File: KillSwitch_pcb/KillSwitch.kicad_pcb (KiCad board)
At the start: 2 copper layers, 93.3 x 68.6 mm, 82 parts, among them IC1 Wio-SX1262, J1 J_ESP_DBG_UART, J2 USB_C_Receptacle_USB2.0, SW1 SW_DIP_x08, SW2 SW_RESET, SW3 SW_BOOT, SW4 ARM, SW5 KILL1, SW6 KILL2, SW7 KILL3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

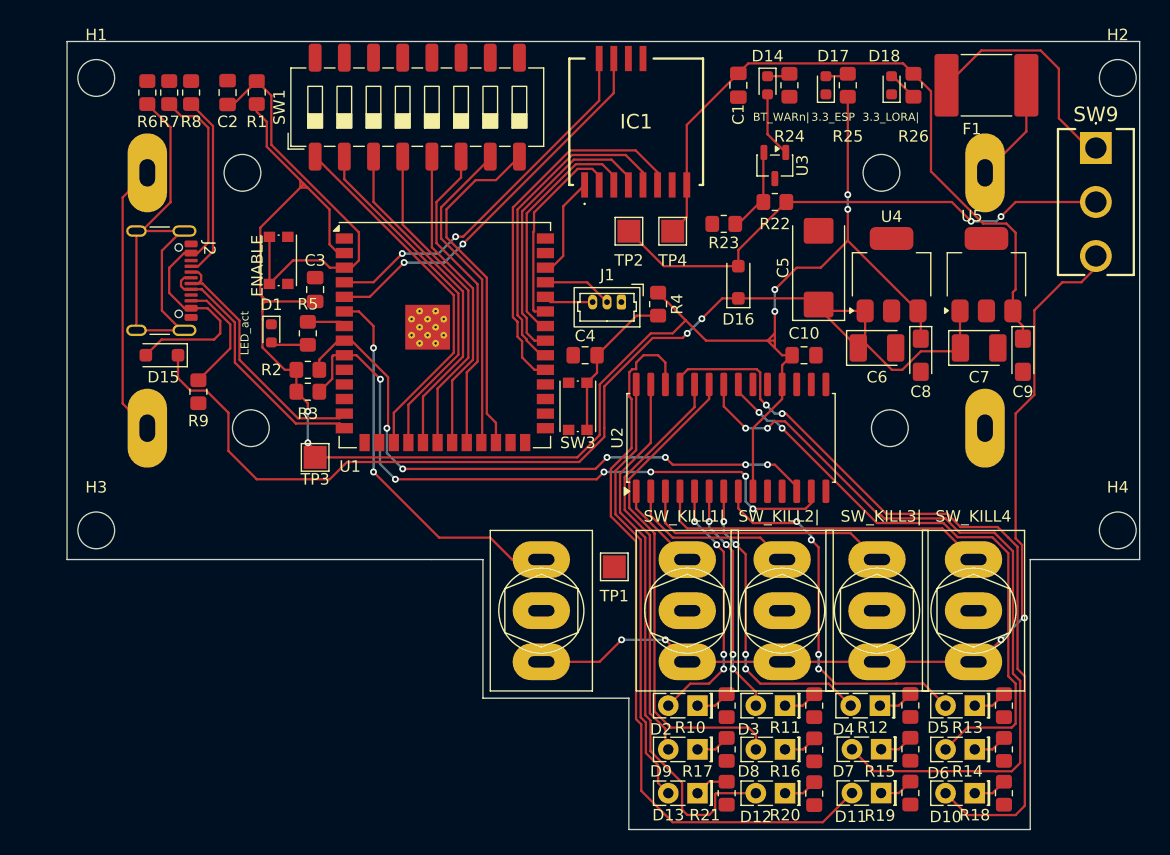
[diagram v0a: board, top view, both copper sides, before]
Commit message: GND+ plus przycięta płytka + Silkscreen + zaokrąglenia
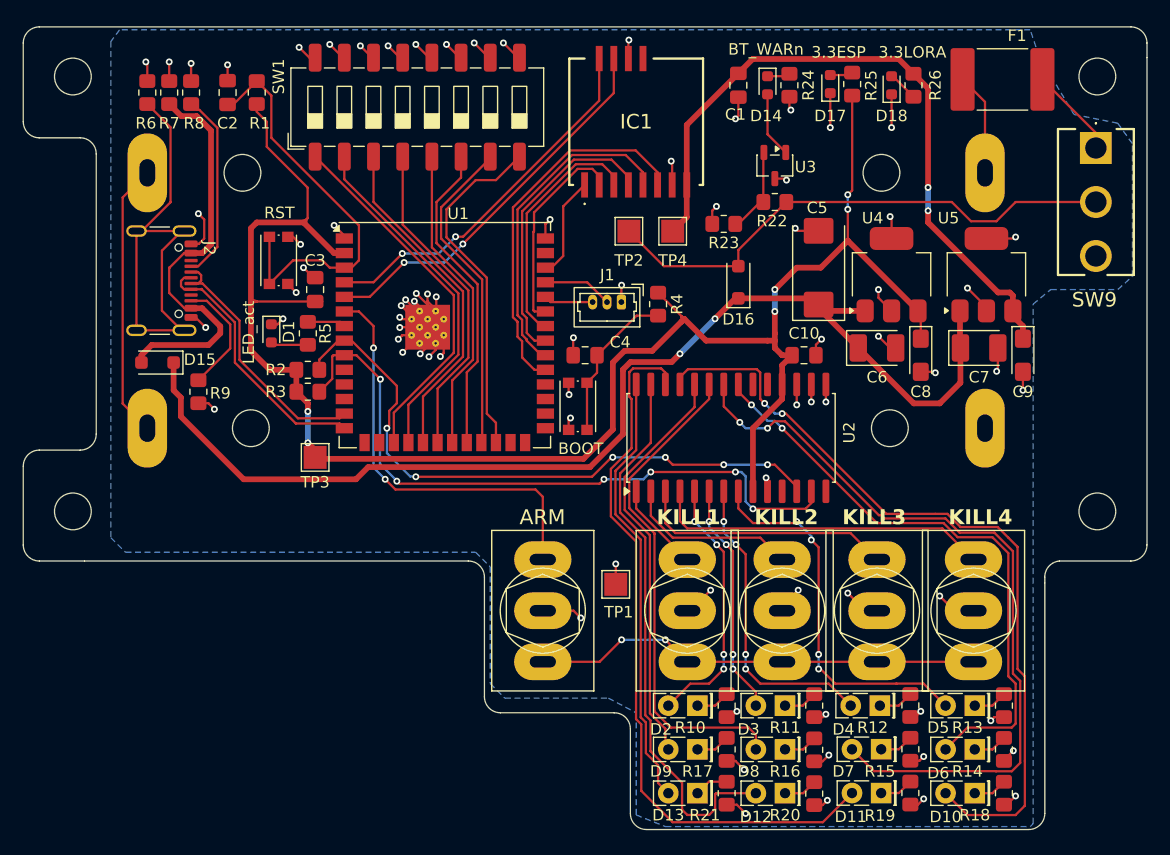
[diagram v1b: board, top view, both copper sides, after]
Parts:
- moved H3 2.62 mm to (126.2, 86.6)
- moved H4 2.43 mm to (215.4, 86.6)
- moved H1 2.04 mm to (126.2, 48.8)
- moved H2 1.78 mm to (215.4, 48.8)
- moved TP1 1.53 mm to (173.5, 93.0)
- moved F1 1.49 mm to (207.1, 49.0), turned to 180 degrees
- moved D15 0.74 mm to (133.6, 73.7)
- moved D17 0.39 mm to (192.2, 49.4)
- moved R25 0.39 mm to (194.1, 49.4)
- moved SW4 0.13 mm to (167.1, 95.3)
- renumbered SW3 to BOOT
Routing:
- net GND: track 0.00 -> 141.8 mm, vias 0 -> 78
- net (no net): track 82.8 -> 41.5 mm, vias 4 -> 2
- net Net-(SW9-A): track 20.3 -> 7.90 mm
- net /SW_ARM: track 33.5 -> 36.6 mm
- net /KillSwitchPower/VIN: track 98.2 -> 100.1 mm
- net /KillSwitchIO/LED_RX2: track 65.1 -> 63.3 mm
- net /KillSwitchIO/SCK: track 53.6 -> 54.8 mm
- net /+VUSB: track 34.6 -> 35.7 mm
- net /+3.3v_LoRa: track 60.8 -> 60.3 mm, vias 0 -> 2
- net /KillSwitchPower/+VBATT: vias 2 -> 0
- added copper zone on B.Cu, net GND
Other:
- board size 93.3 x 68.6 mm -> 97.8 x 69.8 mm
- board text added: "3.3ESP"
- board text added: "3.3LORA"
- board text added: "ARM"
- board text added: "BT_WARn"
- board text added: "KILL1"
- board text added: "KILL2"
- board text added: "KILL3"
- board text added: "KILL4"
- board text added: "RST"
- board text removed: "3.3_ESP"
- board text removed: "3.3_LORA|"
- board text removed: "BT_WARn|"
- board text removed: "ENABLE"
- board text removed: "SW_KILL1|"
- board text removed: "SW_KILL2|"
- board text removed: "SW_KILL3|"
- board text removed: "SW_KILL4"

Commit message: poprawiony silkskrin
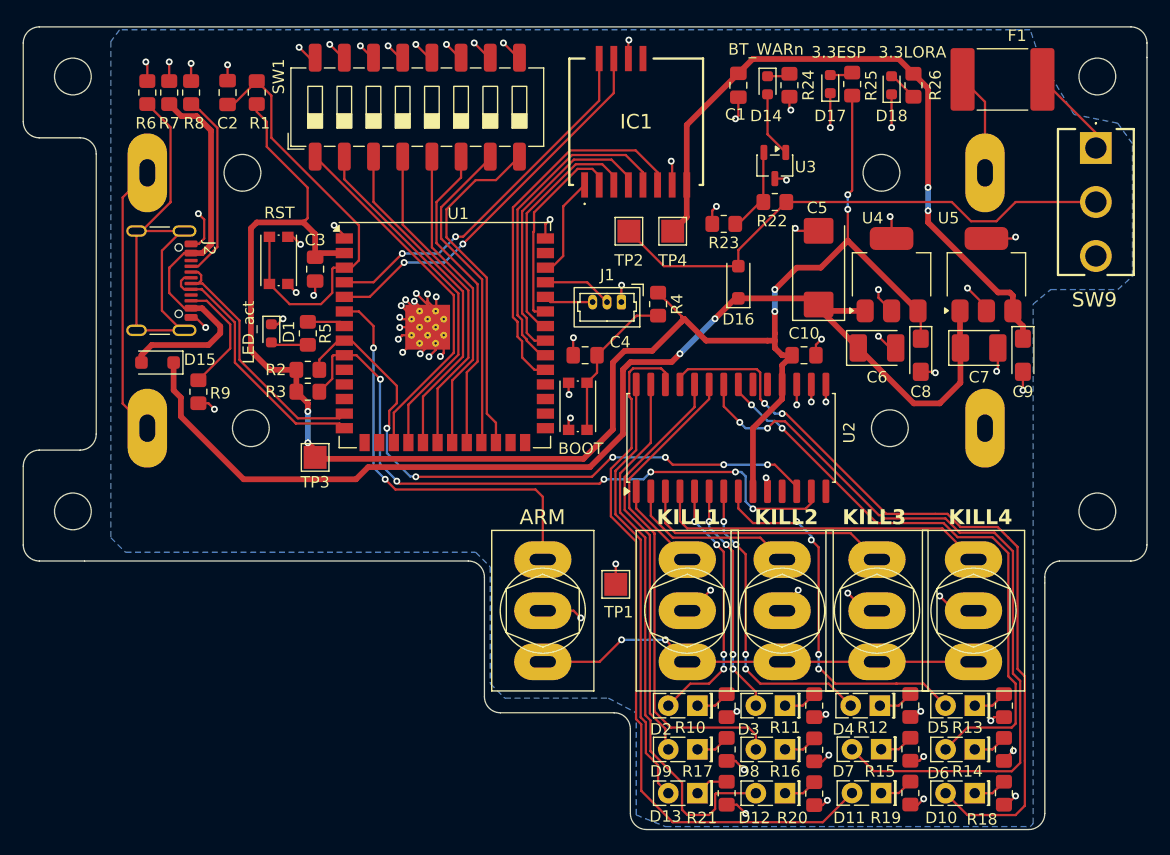
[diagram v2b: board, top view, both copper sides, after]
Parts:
- moved C3 1.78 mm to (147.3, 65.5), turned to 90 degrees
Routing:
- net /+3.3v_ESP: track 156.8 -> 152.0 mm
- net /ENABLE: track 35.9 -> 38.1 mm
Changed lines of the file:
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@@
 		(tags "LED")
 		(property "Reference" "D13"
-			(at 2.54 -1.905 0)
+			(at 2.7931 -2.0181 0)
 			(layer "F.SilkS")
 			(effects
@@
 	(footprint "Capacitor_SMD:C_0805_2012Metric_Pad1.18x1.45mm_HandSolder"
 		(layer "F.Cu")
-		(at 147.32 67.31 -90)
+		(at 147.32 65.532 90)
 		(descr "Capacitor SMD 0805 (2012 Metric), square (rectangular) end terminal, IPC-7351 nominal with elongated pad for handsoldering. (Body size source: IPC-SM-782 page 76, https://www.pcb-3d.com/wordpress/wp-content/uploads/ipc-sm-782a_amendment_1_and_2.pdf, https://docs.google.com/spreadsheets/d/1BsfQQcO9C6DZCsRaXUlFlo91Tg2WpOkGARC1WS5S8t0/edit?usp=sharing), generated with kicad-footprint-generator")
 		(tags "capacitor handsolder")
 		(property "Reference" "C3"
-			(at -2.54 0 180)
+			(at 2.54 0 0)
 			(layer "F.SilkS")
 			(effects
@@
 		(attr smd)
 		(fp_line
-			(start -0.261252 0.735)
-			(end 0.261252 0.735)
+			(start -0.261252 -0.735)
+			(end 0.261252 -0.735)
 			(stroke
 				(width 0.12)
@@
 		)
 		(fp_line
-			(start -0.261252 -0.735)
-			(end 0.261252 -0.735)
+			(start -0.261252 0.735)
+			(end 0.261252 0.735)
 			(stroke
 				(width 0.12)
@@
 		)
 		(pad "1" smd roundrect
-			(at -1.0375 0 270)
+			(at -1.0375 0 90)
 			(size 1.175 1.45)
 			(layers "F.Cu" "F.Mask" "F.Paste")
@@
 		)
 		(pad "2" smd roundrect
-			(at 1.0375 0 270)
+			(at 1.0375 0 90)
 			(size 1.175 1.45)
 			(layers "F.Cu" "F.Mask" "F.Paste")
@@
 		(tags "LED")
 		(property "Reference" "D11"
-			(at 2.6519 -2.06 0)
+			(at 2.778 -2.159 0)
 			(layer "F.SilkS")
 			(effects
@@
 		(tags "resistor handsolder")
 		(property "Reference" "R19"
-			(at 1.9579 2.6519 180)
+			(at 2.159 2.143 180)
 			(layer "F.SilkS")
 			(effects
@@
 		(tags "resistor handsolder")
 		(property "Reference" "R18"
-			(at 1.905 2.54 180)
+			(at 2.2721 1.9041 180)
 			(layer "F.SilkS")
 			(effects
@@
 		(tags "LED")
 		(property "Reference" "D10"
-			(at 2.54 -2.06 0)
+			(at 2.9201 -2.1451 0)
 			(layer "F.SilkS")
 			(effects
@@
 		(tags "resistor handsolder")
 		(property "Reference" "R21"
-			(at 1.905 1.905 180)
+			(at 2.1451 2.1581 180)
 			(layer "F.SilkS")
 			(effects
@@
 		(tags "resistor handsolder")
 		(property "Reference" "R20"
-			(at 1.869 2.54 180)
+			(at 2.1091 1.9041 180)
 			(layer "F.SilkS")
 			(effects
@@
 		(tags "LED")
 		(property "Reference" "D12"
-			(at 2.54 -2.06 0)
+			(at 2.6661 -2.1451 0)
 			(layer "F.SilkS")
 			(effects
@@
 	)
 	(gr_line
-		(start 142.24 68.3475)
-		(end 141.859 68.453)
-		(stroke
-			(width 0.2)
-			(type default)
-		)
-		(layer "F.Cu")
-		(net 6)
-	)
-	(gr_line
 		(start 157.988 70.612)
 		(end 157.861 70.612)
@@
 	(gr_line
 		(start 146.558 61.214)
-		(end 146.558 61.595)
-		(stroke
-			(width 0.2)
-			(type default)
-		)
-		(layer "F.Cu")
-		(net 6)
-	)
-	(gr_line
-		(start 146.558 61.214)
 		(end 146.05 61.468)
 		(stroke
@@
 		(net 6)
 	)
-	(gr_line
-		(start 142.24 68.326)
-		(end 141.859 68.199)
-		(stroke
-			(width 0.2)
-			(type default)
-		)
-		(layer "F.Cu")
-		(net 6)
-	)
 	(gr_arc
 		(start 126.873 54.102)
@@
 	)
 	(segment
-		(start 147.32 66.2725)
-		(end 147.1715 66.2725)
-		(width 0.2)
-		(layer "F.Cu")
-		(net 1)
-	)
-	(segment
 		(start 207.2631 108.3289)
 		(end 207.2631 108.2599)
@@
 	)
 	(segment
+		(start 147.32 66.5695)
+		(end 147.32 67.691)
+		(width 0.2)
+		(layer "F.Cu")
+		(net 1)
+	)
+	(segment
 		(start 149.746 47.13)
 		(end 148.59 45.974)
@@
 	)
 	(segment
-		(start 147.1715 66.2725)
-		(end 146.304 65.405)
-		(width 0.2)
-		(layer "F.Cu")
-		(net 1)
-	)
-	(segment
 		(start 197.485 62.865)
 		(end 197.485 61.087)
@@
 	)
 	(segment
+		(start 147.32 67.691)
+		(end 147.193 67.818)
+		(width 0.2)
+		(layer "F.Cu")
+		(net 1)
+	)
+	(segment
 		(start 157.239 47.13)
 		(end 156.083 45.974)
@@
 	)
 	(via
+		(at 147.193 67.818)
+		(size 0.6)
+		(drill 0.3)
+		(layers "F.Cu" "B.Cu")
+		(net 1)
+	)
+	(via
 		(at 169.418 76.454)
 		(size 0.6)
@@
 	)
 	(via
-		(at 146.304 65.405)
-		(size 0.6)
-		(drill 0.3)
-		(layers "F.Cu" "B.Cu")
-		(net 1)
-	)
-	(via
 		(at 153.67 46.101)
 		(size 0.6)
@@
 	)
 	(segment
+		(start 148.809 67.599)
+		(end 148.809 65.506)
+		(width 0.2)
+		(layer "F.Cu")
+		(net 5)
+	)
+	(segment
 		(start 151.13 64.77)
 		(end 150.495 65.405)
@@
 	)
 	(segment
-		(start 149.86 65.405)
-		(end 148.59 65.405)
+		(start 145.105 68.58)
+		(end 147.828 68.58)
 		(width 0.2)
 		(layer "F.Cu")
@@
 	)
 	(segment
-		(start 143.51 50.435)
-		(end 143.51 54.102)
+		(start 148.91 65.405)
+		(end 149.86 65.405)
 		(width 0.2)
 		(layer "F.Cu")
@@
 	)
 	(segment
-		(start 145.395 64.77)
-		(end 143.345 66.82)
+		(start 147.828 68.58)
+		(end 148.809 67.599)
 		(width 0.2)
 		(layer "F.Cu")
@@
 	)
 	(segment
-		(start 150.495 65.405)
-		(end 149.86 65.405)
+		(start 143.345 66.82)
+		(end 145.105 68.58)
 		(width 0.2)
 		(layer "F.Cu")
@@
 	)
 	(segment
-		(start 140.2025 51.2025)
-		(end 142.24 49.165)
+		(start 143.51 50.435)
+		(end 143.51 54.102)
 		(width 0.2)
 		(layer "F.Cu")
@@
 	)
 	(segment
-		(start 147.955 64.77)
-		(end 145.395 64.77)
+		(start 150.495 65.405)
+		(end 149.86 65.405)
 		(width 0.2)
 		(layer "F.Cu")
@@
 	)
 	(segment
-		(start 148.59 65.405)
-		(end 147.955 64.77)
+		(start 140.2025 51.2025)
+		(end 142.24 49.165)
 		(width 0.2)
 		(layer "F.Cu")
@@
 	)
 	(segment
-		(start 170.670768 82.042)
-		(end 147.447 82.042)
-		(width 0.5)
-		(layer "F.Cu")
-		(net 6)
-	)
-	(segment
-		(start 179.197 69.723)
-		(end 179.197 70.104)
+		(start 148.809 65.506)
+		(end 148.91 65.405)
 		(width 0.2)
 		(layer "F.Cu")
-		(net 6)
+		(net 5)
 	)
 	(segment
-		(start 146.304 61.468)
-		(end 148.971 64.135)
+		(start 170.670768 82.042)
+		(end 147.447 82.042)
 		(width 0.5)
 		(layer "F.Cu")
@@
 	)
 	(segment
-		(start 141.9645 68.3475)
-		(end 141.732 68.58)
+		(start 179.197 69.723)
+		(end 179.197 70.104)
 		(width 0.2)
 		(layer "F.Cu")
@@
 	)
 	(segment
+		(start 147.32 64.4945)
+		(end 147.32 62.484)
+		(width 0.5)
+		(layer "F.Cu")
+		(net 6)
+	)
+	(segment
 		(start 143.109 54.8791)
 		(end 146.66745 58.43755)
@@
 	)
 	(segment
-		(start 148.971 64.135)
-		(end 149.86 64.135)
-		(width 0.5)
-		(layer "F.Cu")
-		(net 6)
-	)
-	(segment
 		(start 193.675 62.865)
 		(end 193.675 60.325)
@@
 	)
 	(segment
-		(start 147.955 68.3475)
-		(end 141.9645 68.3475)
-		(width 0.2)
-		(layer "F.Cu")
-		(net 6)
-	)
-	(segment
 		(start 188.8275 73.025)
 		(end 187.96 73.8925)
@@
 	)
 	(segment
+		(start 149.86 64.135)
+		(end 147.6795 64.135)
+		(width 0.5)
+		(layer "F.Cu")
+		(net 6)
+	)
+	(segment
+		(start 147.6795 64.135)
+		(end 147.32 64.4945)
+		(width 0.2)
+		(layer "F.Cu")
+		(net 6)
+	)
+	(segment
 		(start 187.96 73.8925)
 		(end 187.96 75.565)
@@
 		(width 0.5)
 		(layer "F.Cu")
+		(net 6)
+	)
+	(segment
+		(start 147.32 62.484)
+		(end 146.304 61.468)
+		(width 0.5)
+		(layer "F.Cu")

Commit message: mini poprawki
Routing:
- net /+3.3v_ESP: track 152.0 -> 157.6 mm
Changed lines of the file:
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@@
+	)
+	(segment
+		(start 186.944 71.755)
+		(end 187.325 71.374)
+		(width 0.5)
+		(layer "F.Cu")
+		(net 6)
 	)
 	(segment
@@
 	)
 	(segment
-		(start 179.197 69.723)
-		(end 179.197 70.104)
-		(width 0.2)
+		(start 146.4945 61.6585)
+		(end 146.304 61.468)
+		(width 0.5)
+		(layer "F.Cu")
+		(net 6)
+	)
+	(segment
+		(start 179.443 69.858)
+		(end 179.6335 70.0485)
+		(width 0.5)
+		(layer "F.Cu")
+		(net 6)
+	)
+	(segment
+		(start 193.516 63.214)
+		(end 193.675 63.055)
+		(width 0.5)
 		(layer "F.Cu")
 		(net 6)
@@
 	)
 	(segment
+		(start 179.213 67.58)
+		(end 180.467 68.834)
+		(width 0.2)
+		(layer "F.Cu")
+		(net 6)
+	)
+	(segment
 		(start 194.056 50.4285)
 		(end 194.056 58.674)
@@
 	(segment
 		(start 187.325 71.755)
-		(end 187.325 71.12)
-		(width 0.5)
+		(end 187.325 71.374)
+		(width 0.5)
+		(layer "F.Cu")
+		(net 6)
+	)
+	(segment
+		(start 188.33025 73.52225)
+		(end 187.96 73.8925)
+		(width 0.5)
+		(layer "F.Cu")
+		(net 6)
+	)
+	(segment
+		(start 180.1415 70.0485)
+		(end 179.6335 70.0485)
+		(width 0.2)
 		(layer "F.Cu")
 		(net 6)
@@
 	)
 	(segment
+		(start 177.165 67.58)
+		(end 179.213 67.58)
+		(width 0.2)
+		(layer "F.Cu")
+		(net 6)
+	)
+	(segment
 		(start 145.685 74.295)
 		(end 145.685 76.2)
@@
 	)
 	(segment
-		(start 179.443 69.858)
-		(end 181.34 71.755)
-		(width 0.5)
-		(layer "F.Cu")
-		(net 6)
-	)
-	(segment
-		(start 179.2525 69.6675)
-		(end 179.197 69.723)
-		(width 0.2)
+		(start 179.8875 70.3025)
+		(end 180.1415 70.5565)
+		(width 0.5)
+		(layer "F.Cu")
+		(net 6)
+	)
+	(segment
+		(start 186.944 71.755)
+		(end 187.325 71.755)
+		(width 0.5)
 		(layer "F.Cu")
 		(net 6)
@@
 	)
 	(segment
+		(start 193.834 63.214)
+		(end 193.516 63.214)
+		(width 0.5)
+		(layer "F.Cu")
+		(net 6)
+	)
+	(segment
 		(start 147.32 81.28)
 		(end 146.685 80.645)
@@
 	)
 	(segment
+		(start 187.325 72.136)
+		(end 187.325 71.755)
+		(width 0.5)
+		(layer "F.Cu")
+		(net 6)
+	)
+	(segment
 		(start 173.228 73.66)
 		(end 173.228 79.484768)
@@
 	)
 	(segment
+		(start 194.0245 63.4045)
+		(end 193.675 63.055)
+		(width 0.5)
+		(layer "F.Cu")
+		(net 6)
+	)
+	(segment
 		(start 200.025 69.405)
 		(end 199.785 69.165)
@@
 	(segment
 		(start 188.8275 73.025)
-		(end 187.96 73.8925)
+		(end 188.33025 73.52225)
+		(width 0.5)
+		(layer "F.Cu")
+		(net 6)
+	)
+	(segment
+		(start 194.0245 63.4045)
+		(end 193.834 63.214)
 		(width 0.5)
 		(layer "F.Cu")
@@
 	)
 	(segment
+		(start 180.1495 70.0405)
+		(end 179.8875 70.3025)
+		(width 0.2)
+		(layer "F.Cu")
+		(net 6)
+	)
+	(segment
+		(start 146.558 61.214)
+		(end 146.558 61.595)
+		(width 0.2)
+		(layer "F.Cu")
+		(net 6)
+	)
+	(segment
 		(start 146.66745 61.10455)
 		(end 146.304 61.468)
@@
 	)
 	(segment
+		(start 180.1495 70.0405)
+		(end 180.1415 70.0485)
+		(width 0.2)
+		(layer "F.Cu")
+		(net 6)
+	)
+	(segment
+		(start 180.467 69.723)
+		(end 180.1495 70.0405)
+		(width 0.2)
+		(layer "F.Cu")
+		(net 6)
+	)
+	(segment
 		(start 142.2025 51.2025)
 		(end 142.24 51.165)
@@
 	)
 	(segment
-		(start 179.2525 69.6675)
-		(end 179.443 69.858)
+		(start 186.944 71.755)
+		(end 187.325 72.136)
+		(width 0.5)
+		(layer "F.Cu")
+		(net 6)
+	)
+	(segment
+		(start 180.1415 70.5565)
+		(end 181.34 71.755)
+		(width 0.5)
+		(layer "F.Cu")
+		(net 6)
+	)
+	(segment
+		(start 146.558 61.595)
+		(end 146.4945 61.6585)
 		(width 0.2)
 		(layer "F.Cu")
@@
 	(segment
 		(start 188.8275 73.025)
-		(end 187.96 73.025)
+		(end 188.087 73.025)
 		(width 0.5)
 		(layer "F.Cu")
@@
 	(segment
 		(start 187.325 72.39)
-		(end 187.325 71.755)
+		(end 187.325 72.136)
 		(width 0.5)
 		(layer "F.Cu")
@@
 	(segment
 		(start 199.785 69.165)
-		(end 193.675 63.055)
+		(end 194.0245 63.4045)
 		(width 0.5)
 		(layer "F.Cu")
@@
 	)
 	(segment
+		(start 188.087 73.279)
+		(end 188.087 73.025)
+		(width 0.5)
+		(layer "F.Cu")
+		(net 6)
+	)
+	(segment
 		(start 193.675 63.055)
 		(end 193.675 62.865)
@@
 	)
 	(segment
+		(start 188.087 73.025)
+		(end 187.96 73.025)
+		(width 0.5)
+		(layer "F.Cu")
+		(net 6)
+	)
+	(segment
+		(start 180.467 68.834)
+		(end 180.467 69.723)
+		(width 0.2)
+		(layer "F.Cu")
+		(net 6)
+	)
+	(segment
 		(start 181.34 71.755)
 		(end 186.69 71.755)
@@
 	)
 	(segment
+		(start 180.1415 70.0485)
+		(end 180.1415 70.5565)
+		(width 0.2)
+		(layer "F.Cu")
+		(net 6)
+	)
+	(segment
 		(start 187.96 73.8925)
 		(end 187.96 75.565)
@@
 	)
 	(segment
-		(start 177.165 67.58)
-		(end 179.2525 69.6675)
-		(width 0.2)
+		(start 187.325 71.374)
+		(end 187.325 71.12)
+		(width 0.5)
 		(layer "F.Cu")
 		(net 6)
@@
 	(segment
 		(start 186.69 71.755)
-		(end 187.325 71.755)
+		(end 186.944 71.755)
 		(width 0.5)
 		(layer "F.Cu")
@@
 	(segment
 		(start 147.32 62.484)
-		(end 146.304 61.468)
+		(end 146.4945 61.6585)
 		(width 0.5)
 		(layer "F.Cu")
@@
 	(segment
 		(start 191.325 65.405)
-		(end 193.675 63.055)
+		(end 193.516 63.214)
 		(width 0.5)
 		(layer "F.Cu")
@@
 	)
 	(segment
+		(start 179.6335 70.0485)
+		(end 179.8875 70.3025)
+		(width 0.5)
+		(layer "F.Cu")
+		(net 6)
+	)
+	(segment
+		(start 188.33025 73.52225)
+		(end 188.087 73.279)
+		(width 0.5)
+		(layer "F.Cu")
+		(net 6)
+	)
+	(segment
 		(start 147.447 82.042)
 		(end 147.32 81.915)
@@
 		(start 134.62 51.165)
 		(end 135.67355 52.21855)
-		(width 0.5)
+		(width 0.2)
 		(layer "F.Cu")
 		(net 36)
@@
 		(start 138.26 53.4671)
 		(end 138.26 63.379592)
-		(width 0.5)
+		(width 0.2)
 		(layer "F.Cu")
 		(net 36)
@@
 		(start 137.01145 52.21855)
 		(end 138.26 53.4671)
-		(width 0.5)
+		(width 0.2)
 		(layer "F.Cu")
 		(net 36)
@@
 		(start 138.26 63.379592)
 		(end 137.504592 64.135)
-		(width 0.5)
+		(width 0.2)
 		(layer "F.Cu")
 		(net 36)
@@
 		(start 135.67355 52.21855)
 		(end 137.01145 52.21855)
-		(width 0.5)
+		(width 0.2)
 		(layer "F.Cu")
 		(net 36)
@@
 		(start 137.504592 64.135)
 		(end 136.525 64.135)
-		(width 0.5)
+		(width 0.2)
 		(layer "F.Cu")
 		(net 36)
